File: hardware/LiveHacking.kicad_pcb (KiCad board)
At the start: 2 copper layers, 83.5 x 83.5 mm, 20 parts, among them J1 Conn_01x05, SW1 RST, SW2 SW_Push, SW3 SW_Push, U1 Pico

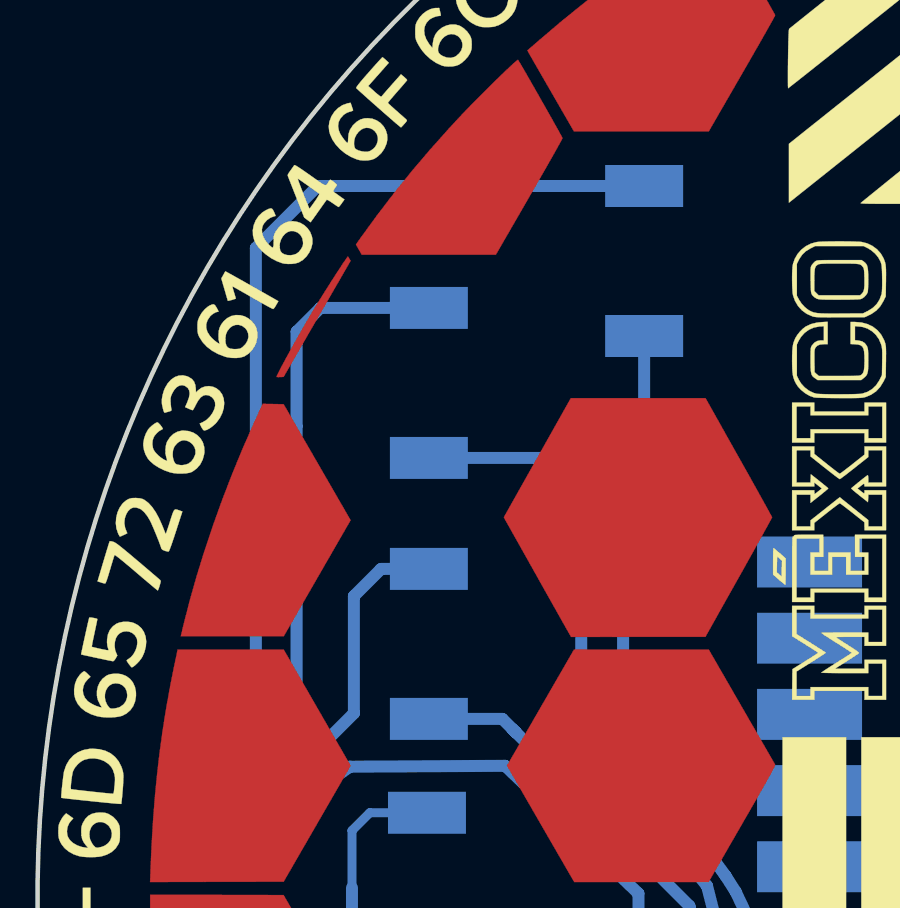
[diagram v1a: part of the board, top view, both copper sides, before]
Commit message: update ground plane
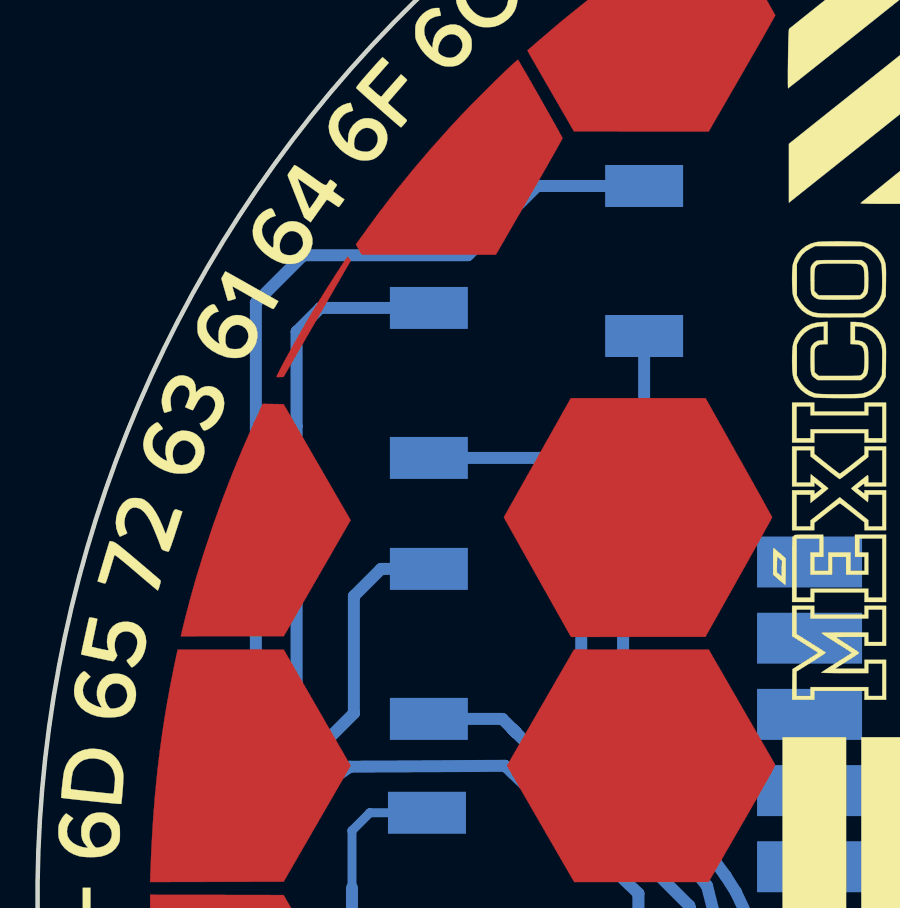
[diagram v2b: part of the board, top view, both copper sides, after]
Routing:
- net Net-(D6-Pad1): track 29.6 -> 28.5 mm
